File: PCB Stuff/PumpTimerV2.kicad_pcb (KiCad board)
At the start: 4 copper layers, 65 x 50 mm, 25 parts, among them J1 1935161, J2 282856-2, J3 282856-2, J4 Conn_02x20_Odd_Even, J6 B4B-PH-SM4-TBT(LF)(SN), K1 ADW1205HLW, K2 ADW1205HLW, Q1 DMN67D7L, Q2 DMN67D7L, SW1 TL3305AF160QG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

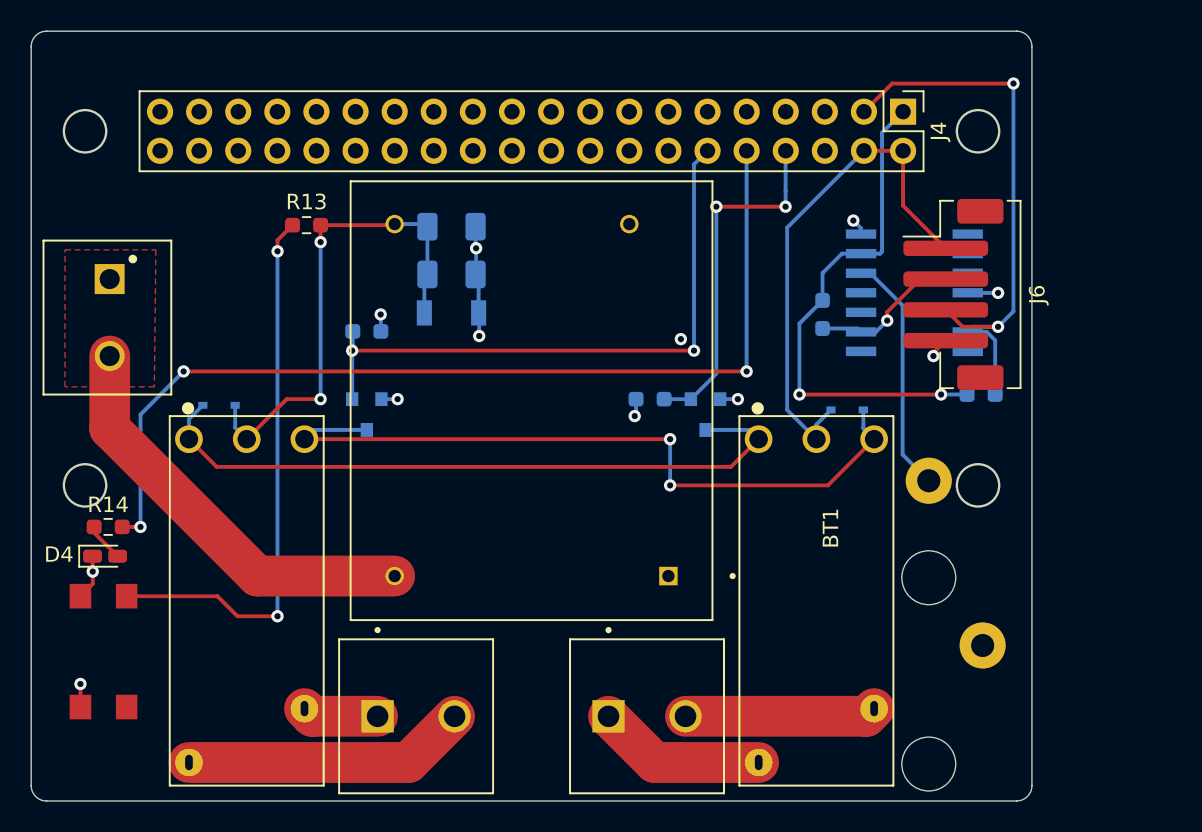
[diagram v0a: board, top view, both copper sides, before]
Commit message: Finished placement and routing. Everything needs reviewed.
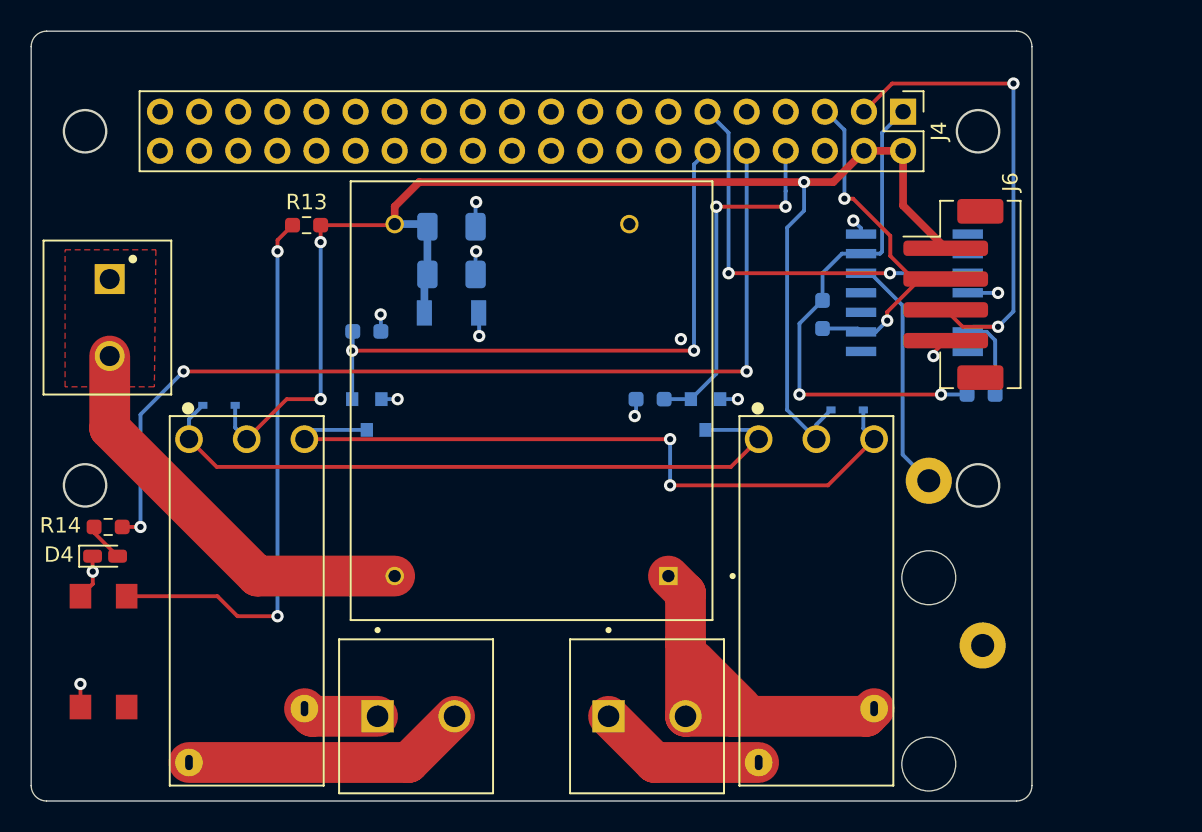
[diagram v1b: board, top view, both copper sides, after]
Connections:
- U1 pad 6: +5VD -> +3V3
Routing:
- net +5VD: track 66.3 -> 95.8 mm, vias 2 -> 3
- net /RTC_~INT~: track 0.00 -> 26.6 mm, vias 0 -> 2
- net /GPIO3(SCL1): track 9.84 -> 25.6 mm, vias 1 -> 2
- net /Line2_in: track 12.5 -> 26.4 mm
- net GND: track 20.5 -> 18.3 mm, vias 11 -> 12

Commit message: Moving battery holder onto tab. Need to add mounting holes at bottom of board and review.
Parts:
- moved BT1 9.00 mm to (107.3, 99.6)
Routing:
- net +BATT: track 15.7 -> 23.5 mm
- net GND: vias 12 -> 35
- net (no net): vias 1 -> 0
- added copper zone on In2.Cu, net GND
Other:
- board size 65 x 50 mm -> 74 x 50 mm

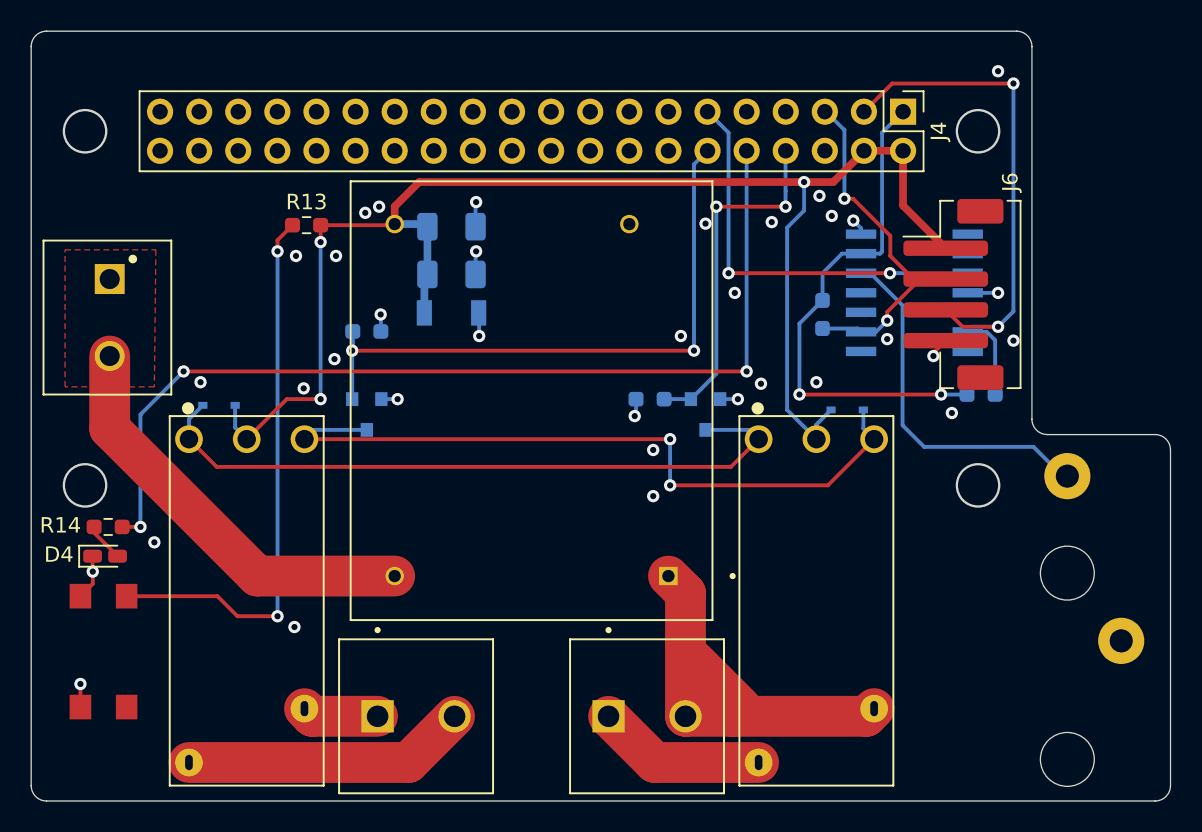
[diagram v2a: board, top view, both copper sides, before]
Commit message: Adding QR code
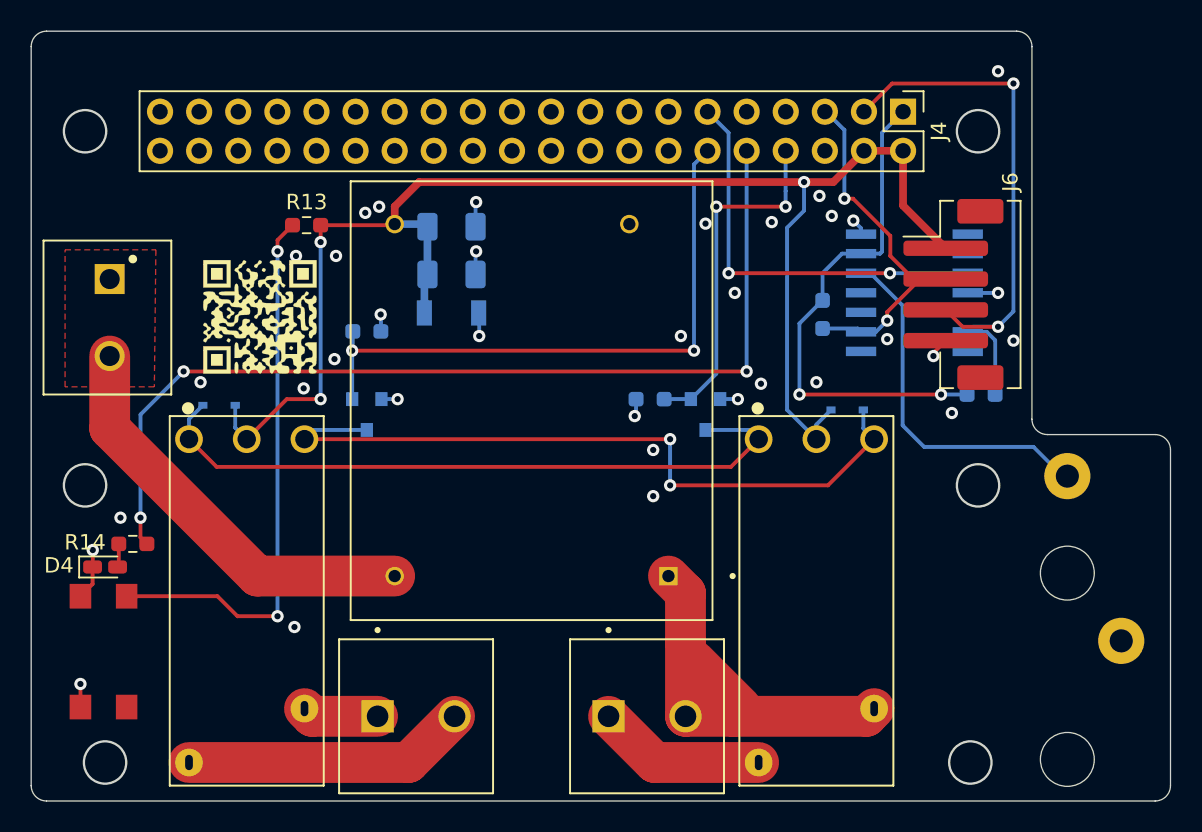
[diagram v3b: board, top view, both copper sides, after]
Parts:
- added G***: LOGO, Footprints:mediumqr, F.Cu at (54.9, 72.6)
- moved R14 1.94 mm to (46.6, 93.3)
- moved D4 0.70 mm to (44.8, 94.8)
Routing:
- net Net-(D4-Pad2): track 2.53 -> 1.53 mm
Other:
- outline, holes or cut-outs redrawn

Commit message: Slight rearranging, changing neutral screw terminal to higher-current model
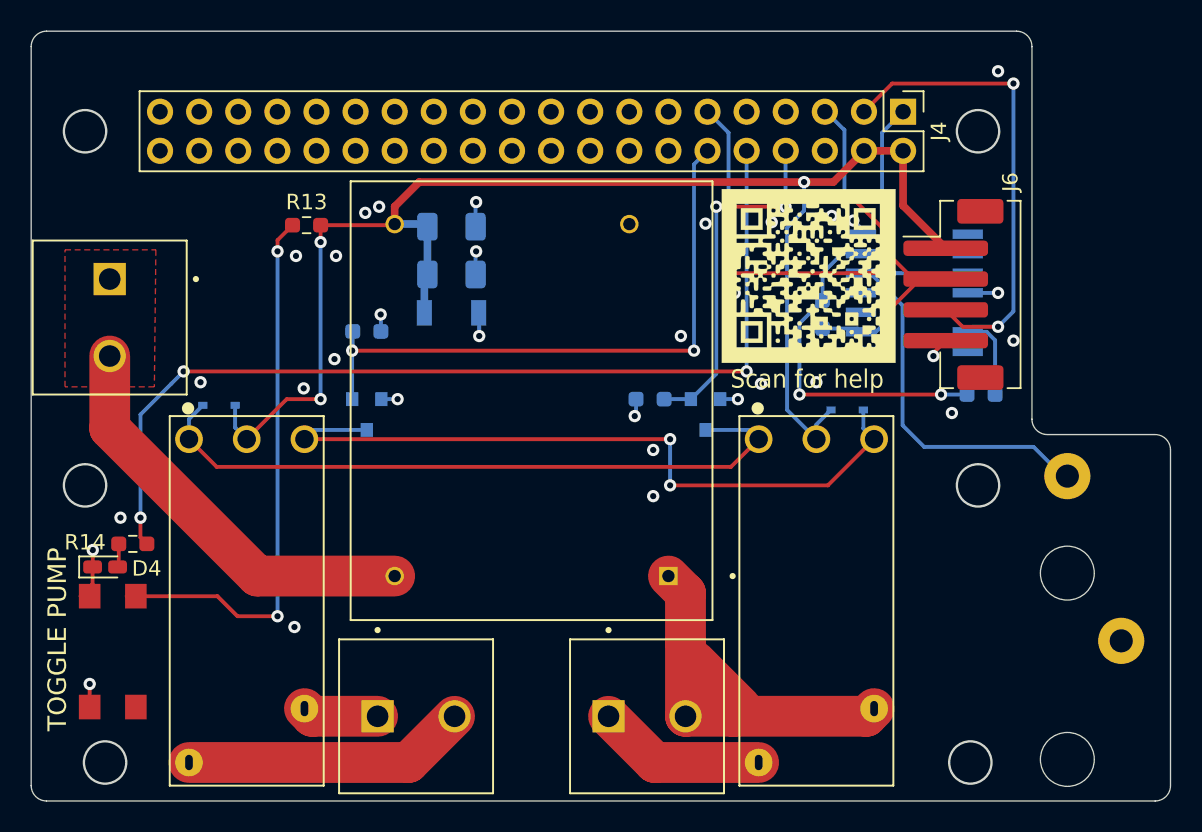
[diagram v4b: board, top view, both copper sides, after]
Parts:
- J1: value 1935161 -> 282856-2; footprint Connector:PHOENIX_1935161 -> Footprints:TE_282856-2
- moved G*** 35.8 mm to (90.5, 75.9)
- moved SW1 0.60 mm to (45.3, 100.3)
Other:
- board text added: "Scan for help"
- board text added: "TOGGLE PUMP"

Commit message: Raspberry Pi header was backwards... Needs rerouted.
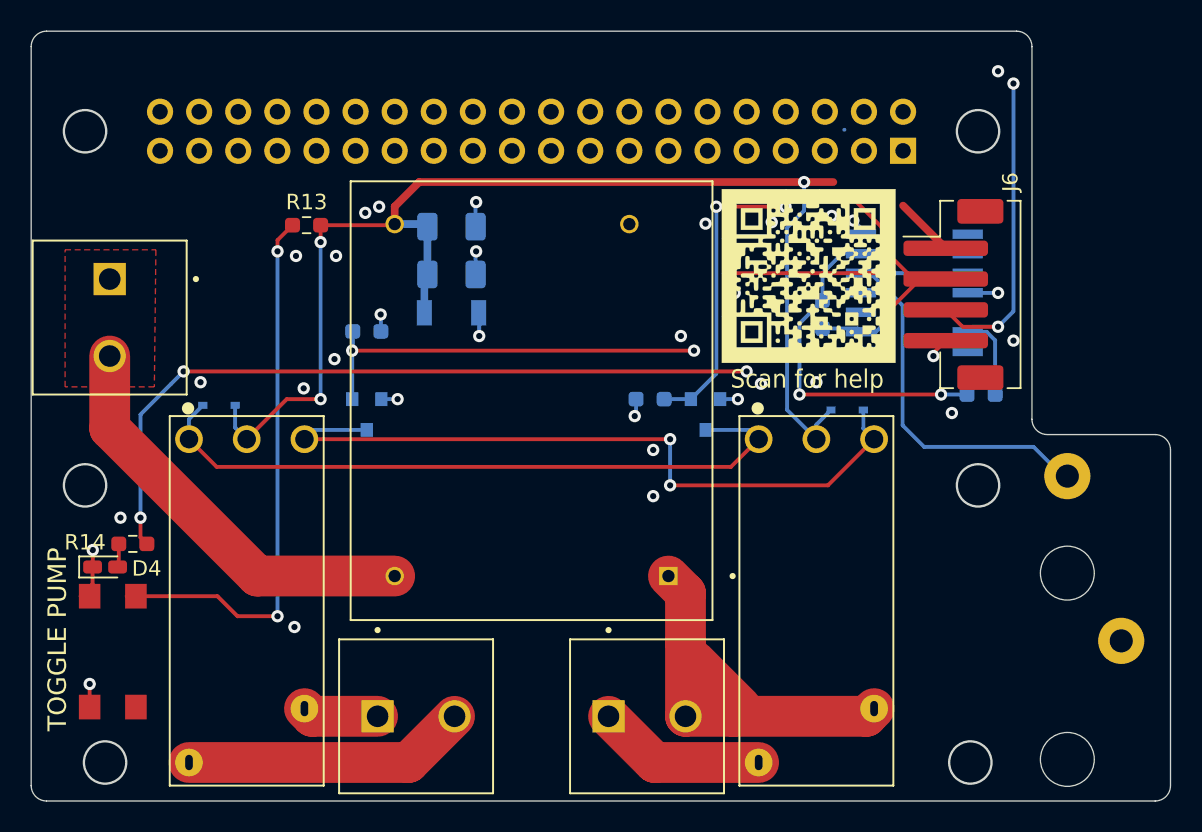
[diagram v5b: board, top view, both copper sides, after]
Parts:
- J4: moved to B.Cu
- moved J4 2.54 mm to (96.6, 67.8), turned to 90 degrees
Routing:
- net /~BTN_RDY~: track 63.4 -> 49.1 mm
- net /RLY_R: track 40.0 -> 26.6 mm
- net /RTC_~INT~: track 26.6 -> 15.5 mm
- net /GPIO2(SDA1): track 38.2 -> 27.7 mm
- net +3V3: track 33.5 -> 23.8 mm
- net +5VD: track 95.8 -> 86.8 mm
- net /GPIO3(SCL1): track 25.6 -> 19.4 mm
- net /RLY_S: track 23.1 -> 19.4 mm

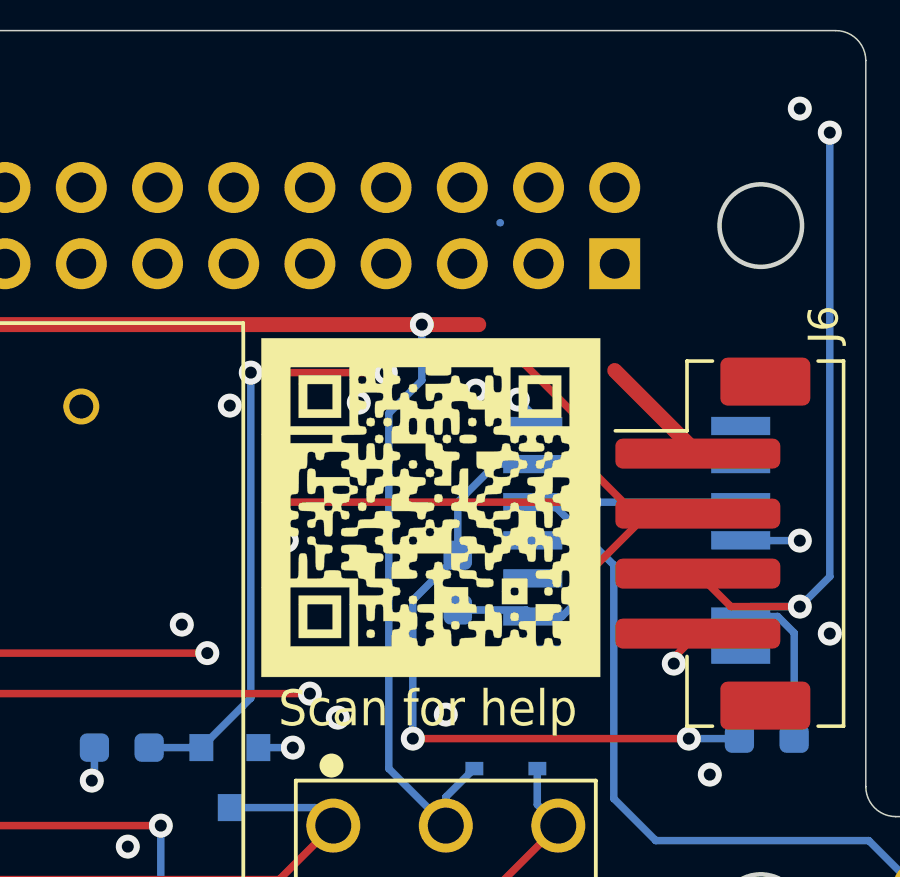
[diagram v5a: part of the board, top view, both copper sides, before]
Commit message: Started re-routing after flipping rpi header
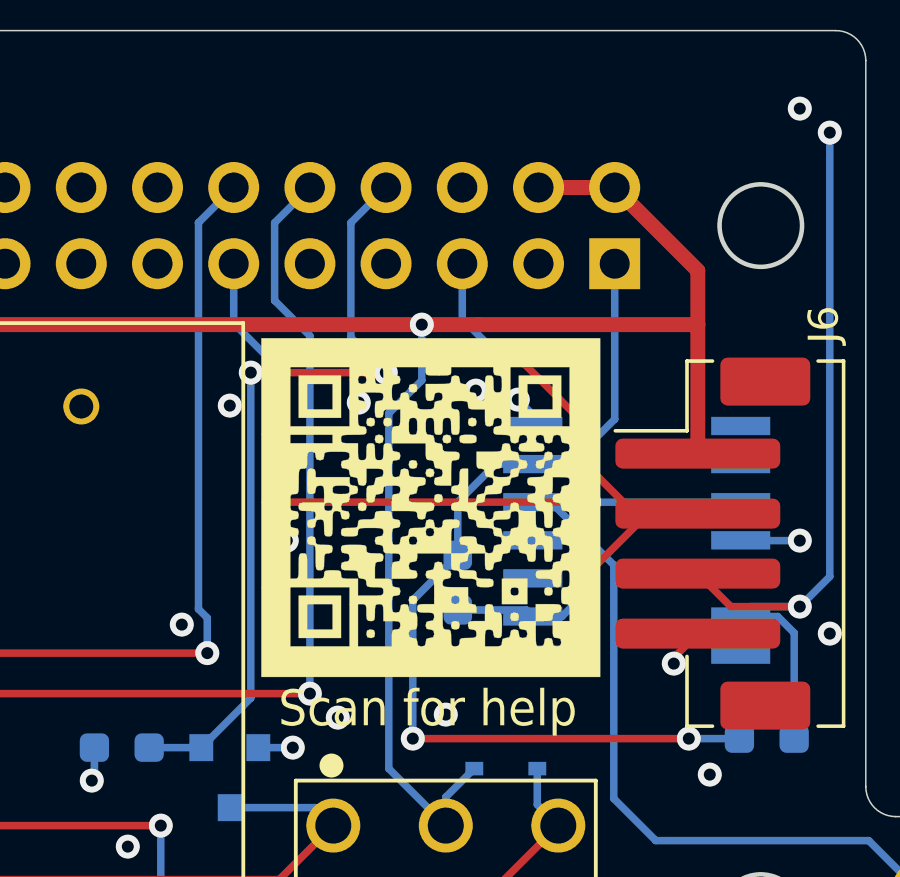
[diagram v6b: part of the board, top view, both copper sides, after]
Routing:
- net /~BTN_RDY~: track 49.1 -> 66.9 mm
- net /RLY_R: track 26.6 -> 42.7 mm
- net +5VD: track 86.8 -> 102.8 mm
- net /RTC_~INT~: track 15.5 -> 24.1 mm
- net /RLY_S: track 19.4 -> 26.6 mm
- net +3V3: track 23.8 -> 31.0 mm
- net /GPIO3(SCL1): track 19.4 -> 23.0 mm
- net (no net): vias 0 -> 1

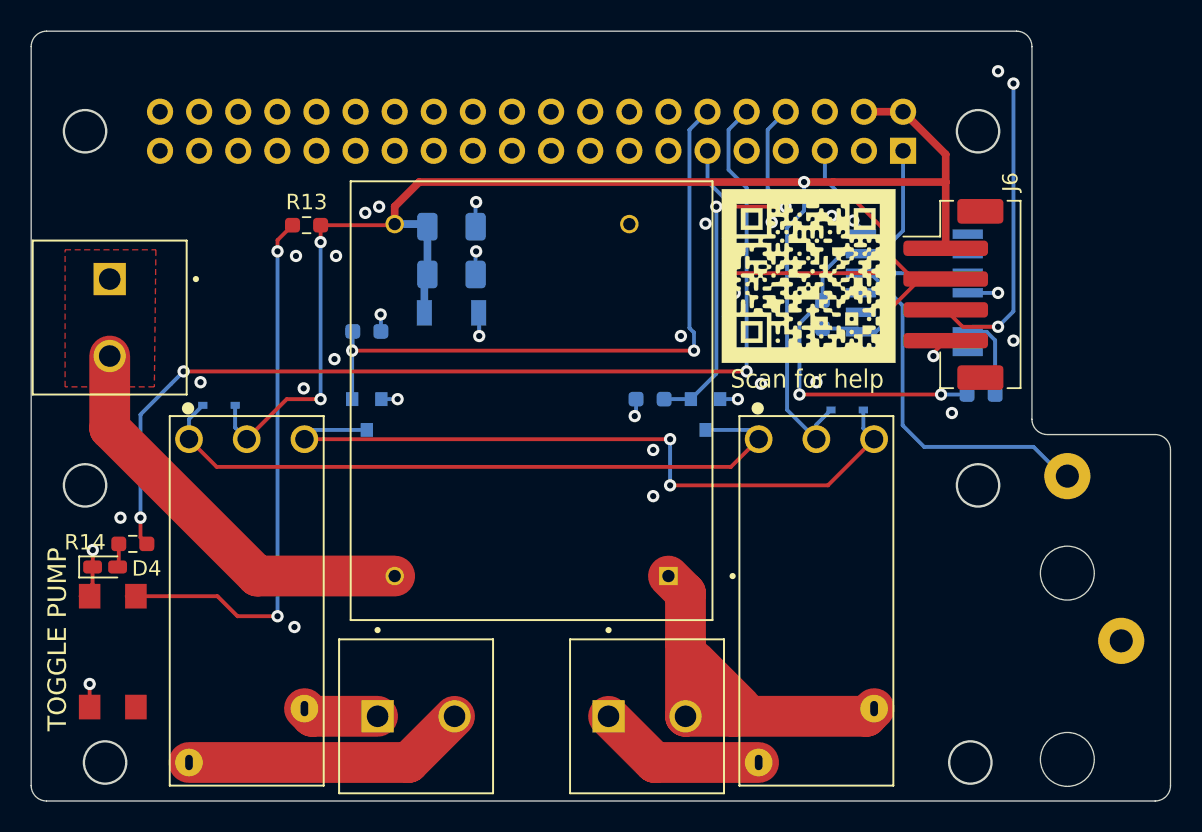
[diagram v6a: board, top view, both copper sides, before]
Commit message: Making sure schematic and PCB match. Finished re-routing after flipping rpi header.
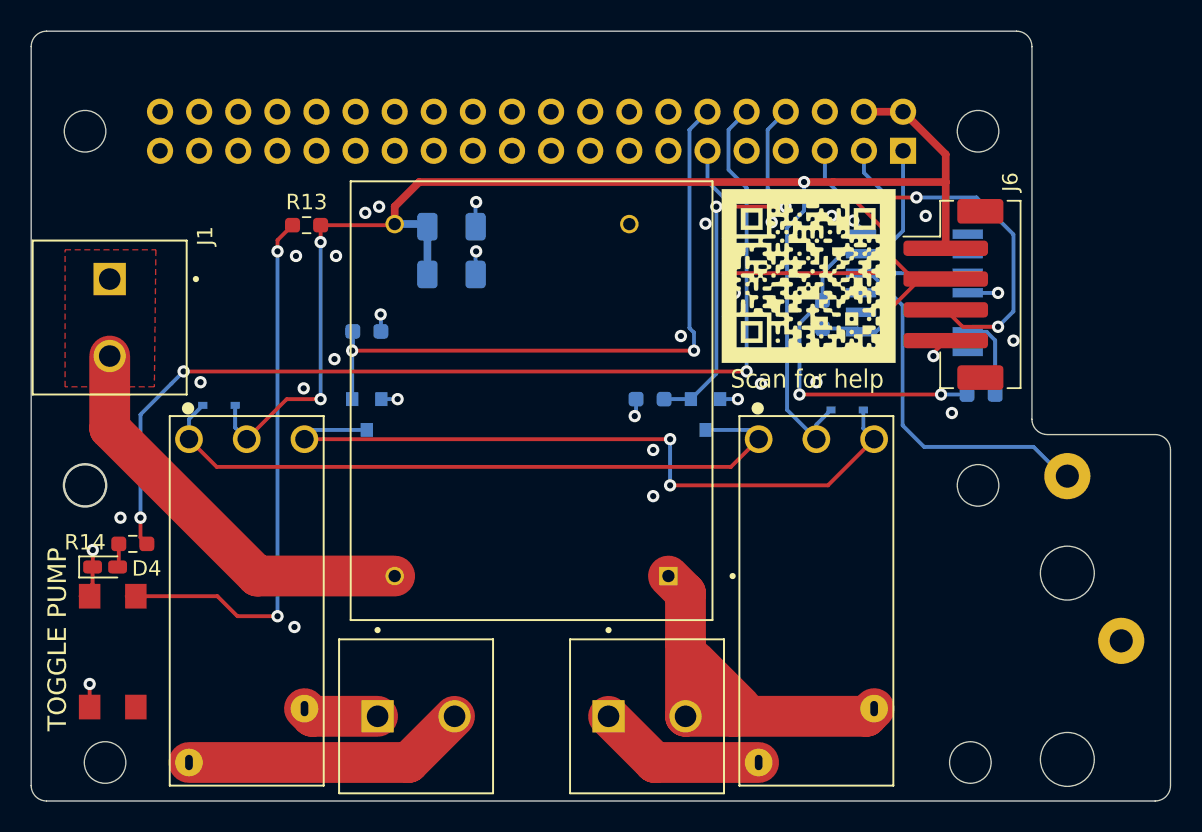
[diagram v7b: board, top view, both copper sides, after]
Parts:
- removed D2: LL4150GS18, Diode_SMD:D_SOD-80
- added H1: 2.75mm Mount, MountingHole:MountingHole_2.7mm_M2.5, F.Cu at (101.5, 66.5)
- added H2: 2.75mm Mount, MountingHole:MountingHole_2.7mm_M2.5, F.Cu at (101.5, 89.5)
- added H3: 2.75mm Mount, MountingHole:MountingHole_2.7mm_M2.5, F.Cu at (43.5, 66.5)
- added H4: 2.75mm Mount, MountingHole:MountingHole_2.7mm_M2.5, F.Cu at (44.8, 107.5)
- added H5: 2.75mm Mount, MountingHole:MountingHole_2.7mm_M2.5, F.Cu at (43.5, 89.5)
- added H6: 2.75mm Mount, MountingHole:MountingHole_2.7mm_M2.5, F.Cu at (101.0, 107.5)
- J1: footprint Footprints:TE_282856-2 -> Connector:TE_282856-2
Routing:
- net /GPIO2(SDA1): track 27.7 -> 30.7 mm, vias 2 -> 3
- net +5VD: track 102.8 -> 100.5 mm
- net GND: track 18.7 -> 17.2 mm
- net (no net): vias 1 -> 0
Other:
- outline, holes or cut-outs redrawn
